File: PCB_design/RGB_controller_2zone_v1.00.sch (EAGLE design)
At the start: 24 parts, among them Q1 IRF512, Q2 IRF512, Q3 IRF512, Q4 IRF512, Q5 IRF512, Q6 IRF512

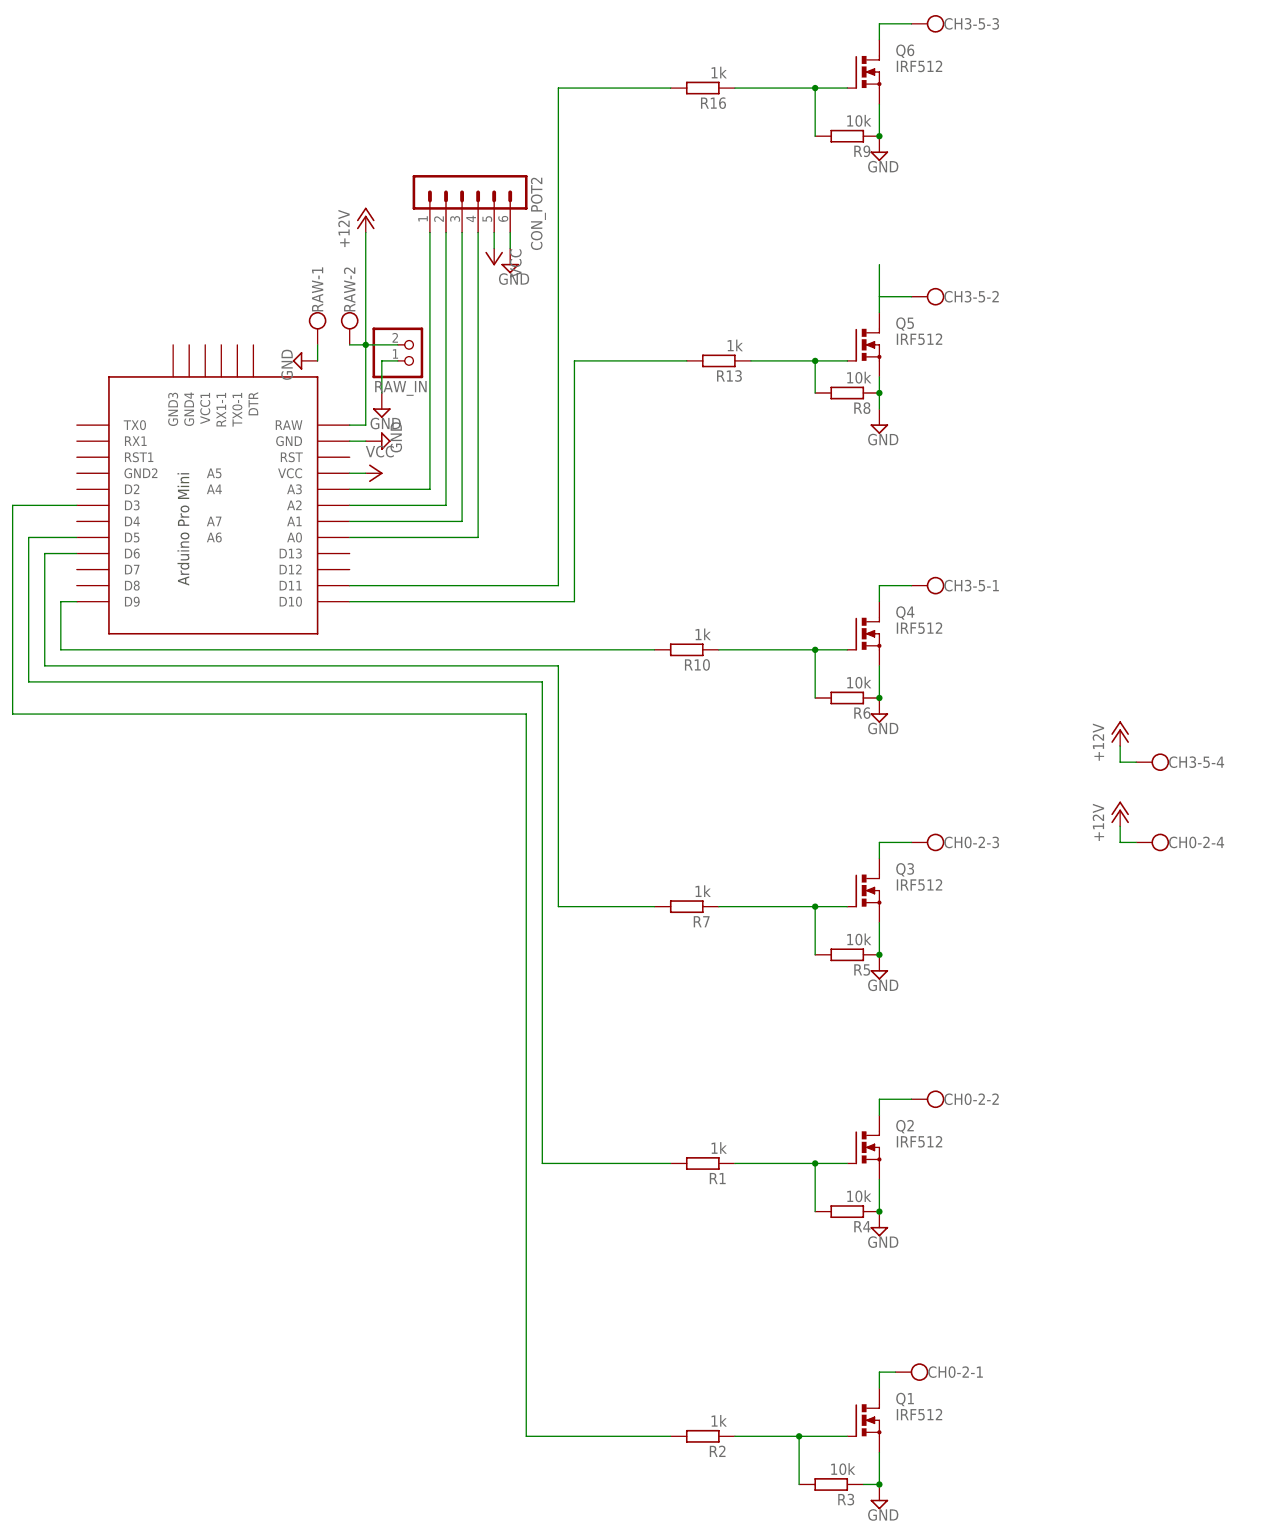
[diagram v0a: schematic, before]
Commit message: Change arduino layout to fit to the buyable clone
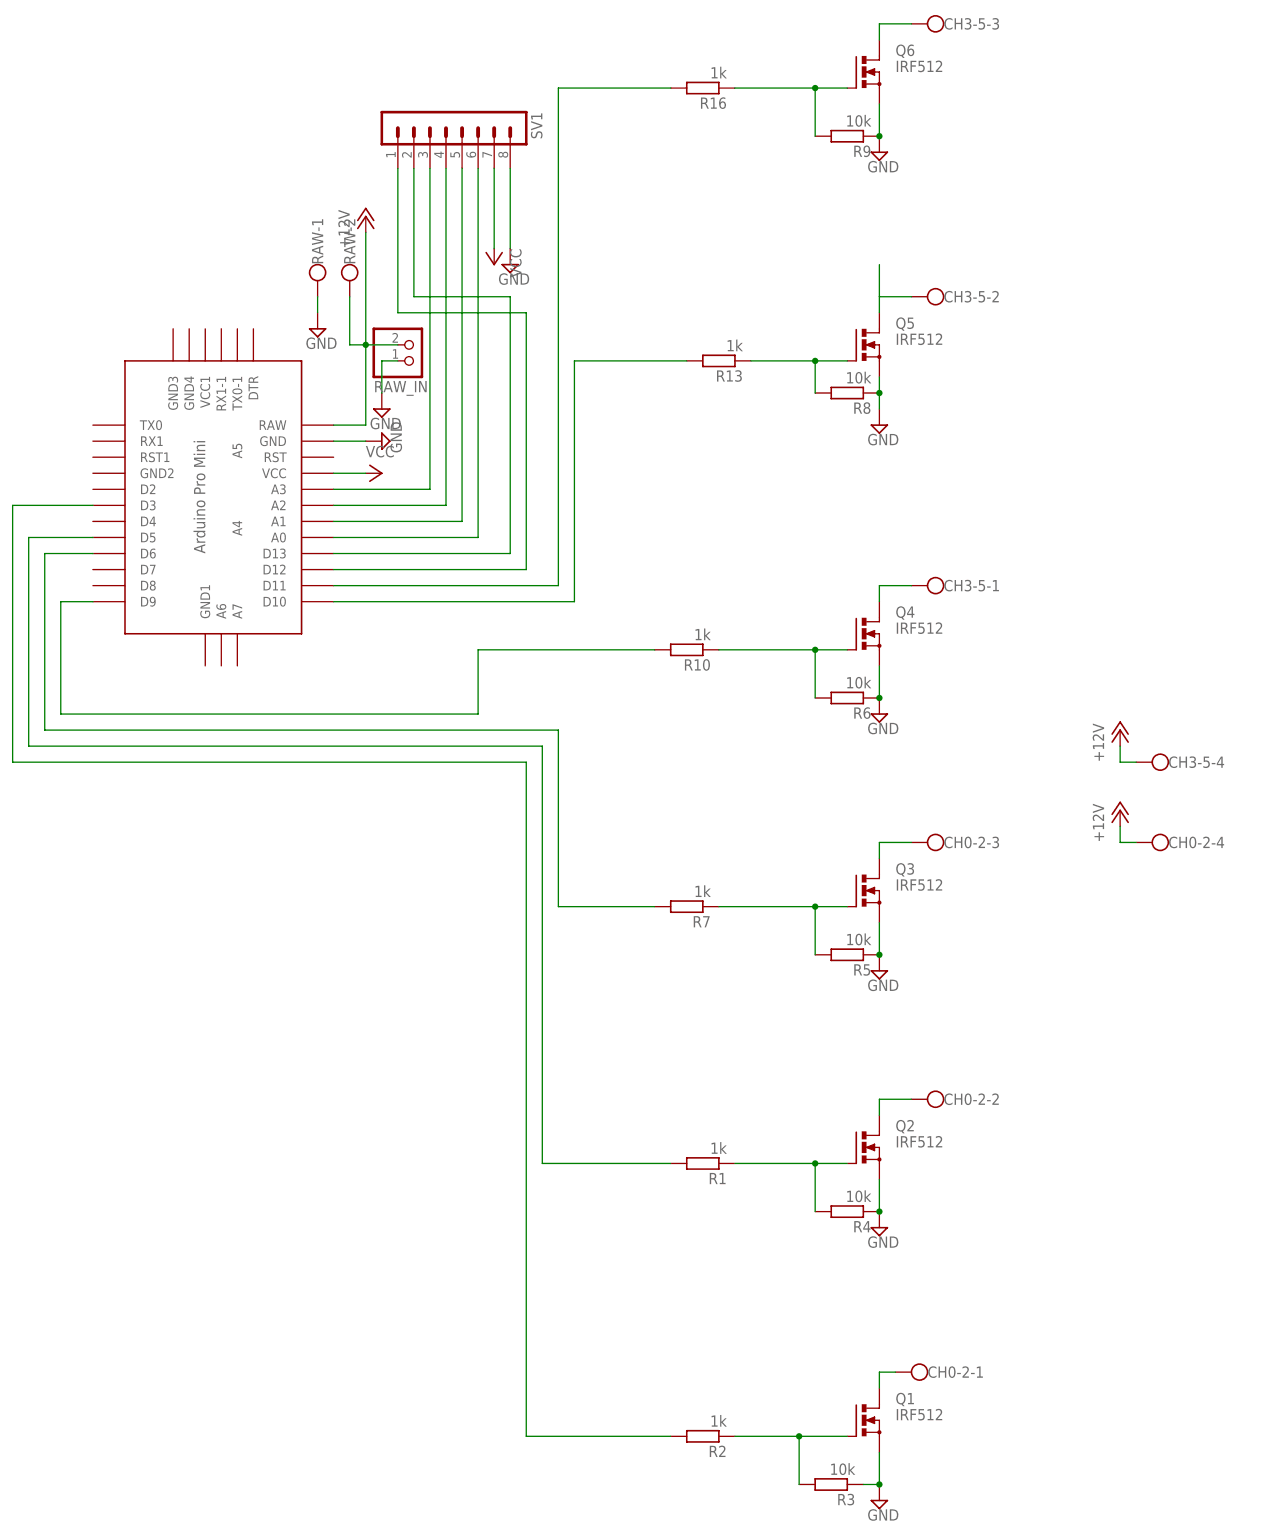
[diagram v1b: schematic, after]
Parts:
- removed CON_POT2: (no value), con-lstb:MA06-1
- added SV1: (no value), con-lstb:MA08-1
- U$1: value PRO-MINI-2 -> ABK-PRO-MINI; device Arduino-clone:PRO-MINI-2 -> Arduino-clone:ABK-PRO-MINI
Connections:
- new net D12: SV1.1, U$1.D12
- new net D13: SV1.2, U$1.D13
- net A0: now also SV1.6; no longer CON_POT2.4
- net A1: now also SV1.5; no longer CON_POT2.3
- net A2: now also SV1.4; no longer CON_POT2.2
- net A3: now also SV1.3; no longer CON_POT2.1
- net GND: now also SV1.8; no longer CON_POT2.6
- net VCC: now also SV1.7; no longer CON_POT2.5
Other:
- moved on the sheet: RAW-1, RAW-2
